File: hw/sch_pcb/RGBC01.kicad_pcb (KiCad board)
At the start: 2 copper layers, 40.1 x 9.7 mm, 19 parts, among them J1 JUMP_5X2, J2 CONN1_1, J3 CONN1_2, J4 CONN1_1, J5 CONN1_1, J6 CONN1_1, J7 CONN1_1, M1 HOLE, M2 HOLE, X1 TCS37717

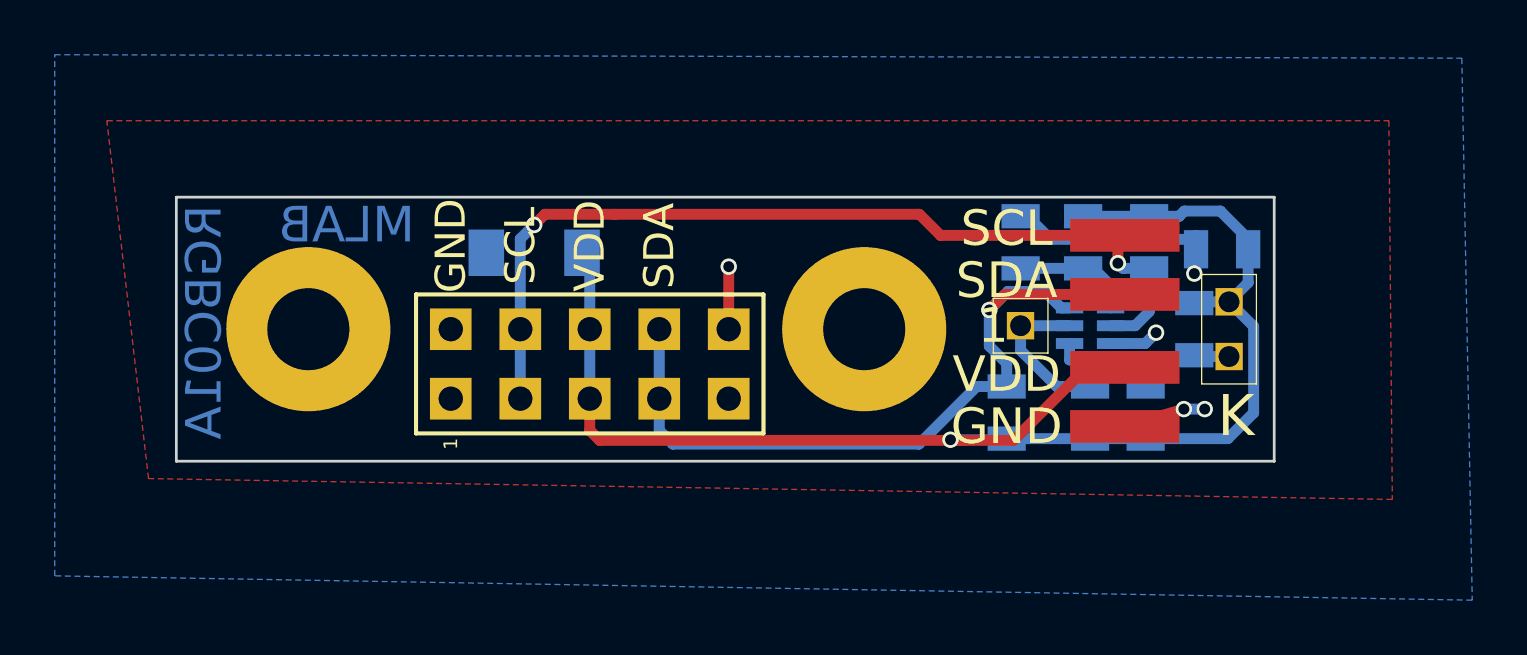
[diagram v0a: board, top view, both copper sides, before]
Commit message: Convert project to KiCAD 7.
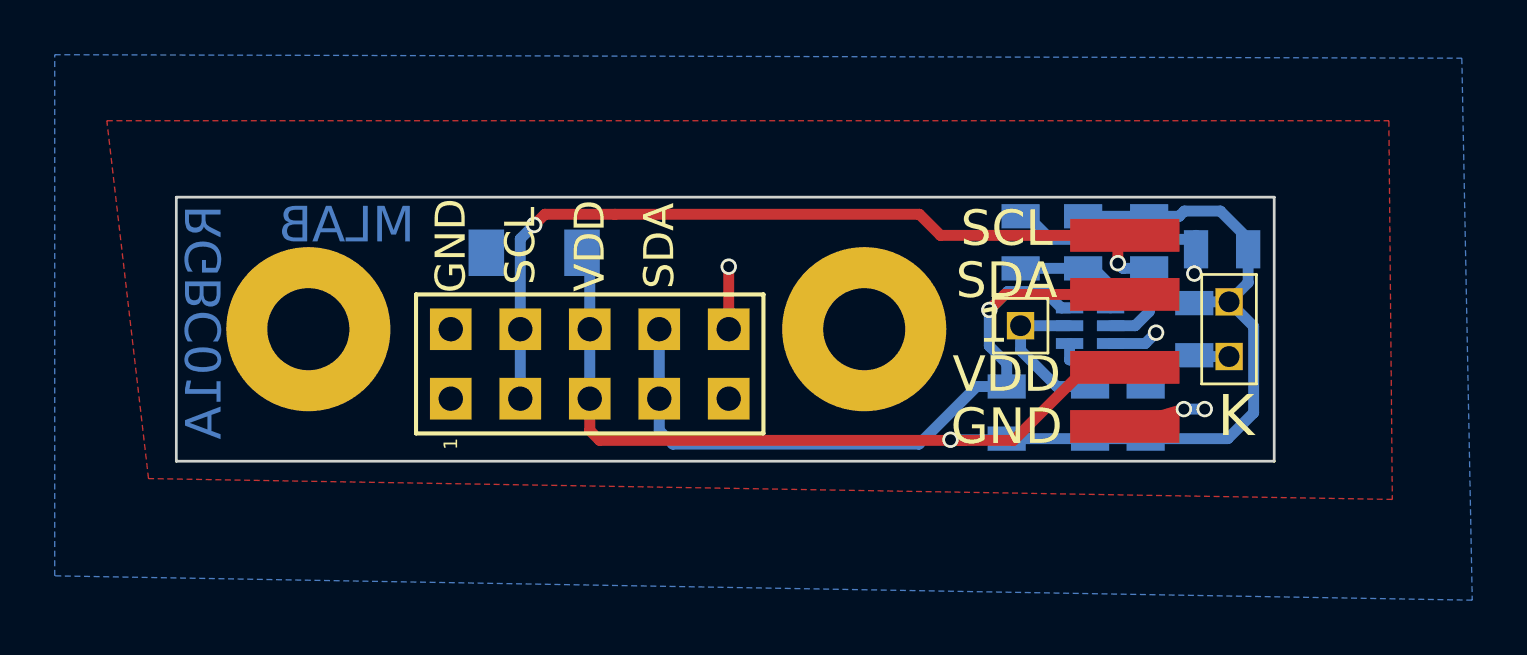
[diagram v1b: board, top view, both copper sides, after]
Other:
- net class Default removed
